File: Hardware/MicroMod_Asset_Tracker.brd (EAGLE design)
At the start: 76.2 x 76.2 mm, 338 parts, among them IC1 SN74AVC4T774PW, IC2 SN74AVC4T774PW, IC3 SN74AVC4T774PW, J11 microSD, J13 TP, J17 NANO_SIM, J18 SARA_USB, J19 NI, J2 JTAG, J4 MICROMOD-2222-C, J5 SPI, J6 DIAG, J7 QWIIC_RIGHT_ANGLE, J9 !RST!, Q1 310mA/60V/1.6Ω, Q10 20V/0.2A/8MHz/1.2Ω/1Vth, Q2 310mA/60V/1.6Ω, Q3 310mA/60V/1.6Ω, Q4 310mA/60V/1.6Ω, Q5 20V/0.2A/8MHz/1.2Ω/1Vth, Q6 20V/4.2A/52mΩ/1.4W, Q7 310mA/60V/1.6Ω, Q8 310mA/60V/1.6Ω, Q9 310mA/60V/1.6Ω, U1 SARA-R5, U13 9DoF IMU, U14 1.8V/100mA, U2 MCP73831, U3 3.3V, U5 AP7361C-33FGE, U7 PCA9306, U8 74HC1G04

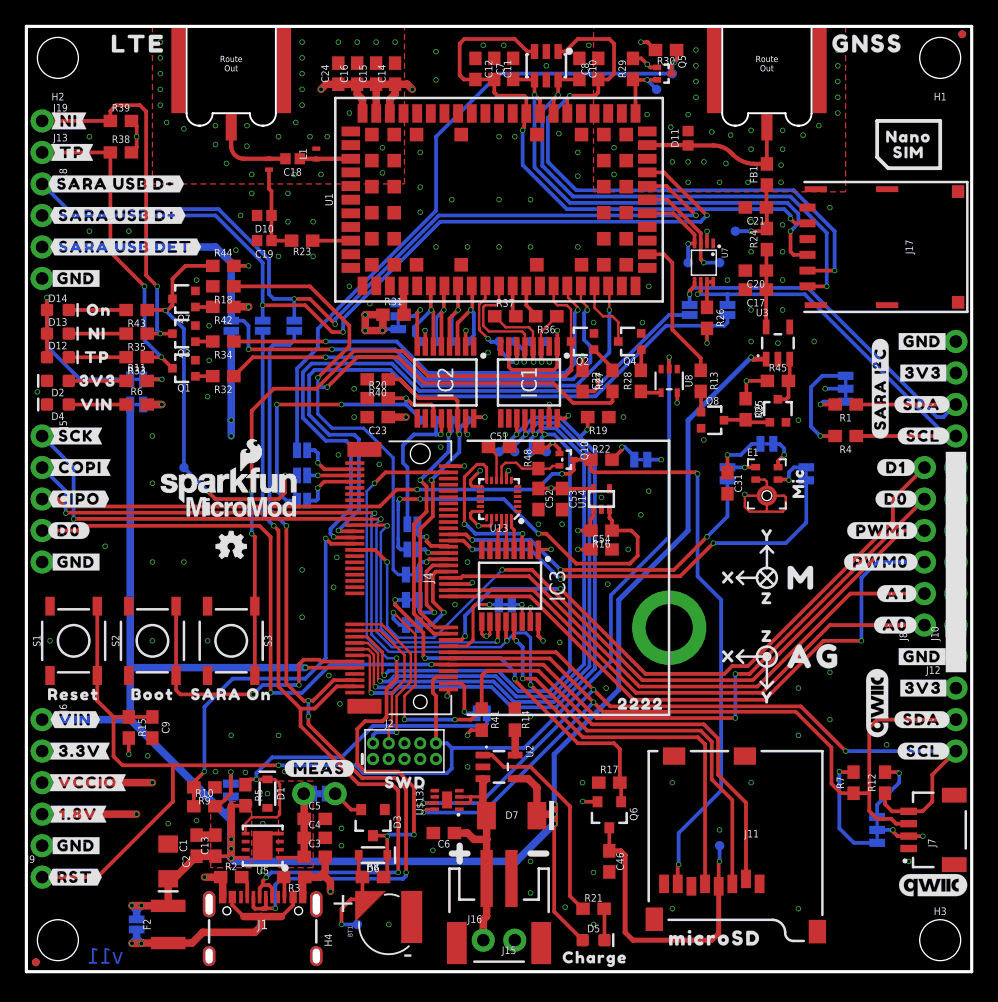
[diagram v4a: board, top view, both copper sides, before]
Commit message: Updated files for v11 after production review
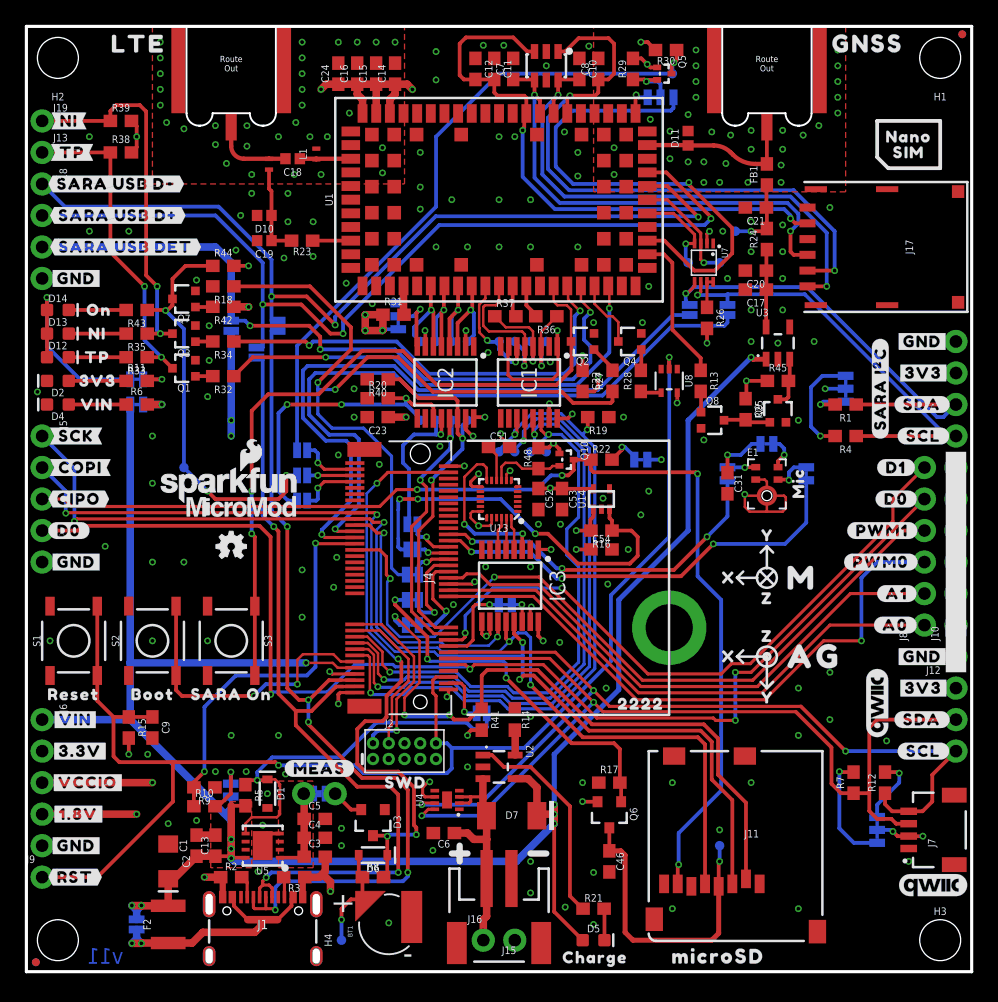
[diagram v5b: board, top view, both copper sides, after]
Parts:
- removed TP11: TEST-POINT3, SparkFun-Connectors:PAD.03X.03
- added JP19: JUMPER-SMT_3_1-NC_TRACE_SILK, SparkFun-Jumpers:SMT-JUMPER_3_1-NC_TRACE_SILK
- added U$118: (no value), output:#EXT_INT#0
- added U$119: (no value), output:#GPIO3#0
- moved U$93 2.22 mm to (18.5, 46.0)
- moved JP4 2.22 mm to (18.5, 49.9)
- moved TP24 1.80 mm to (25.4, 2.54)
- moved U$28 1.48 mm to (51.1, 1.24)
- moved JP3 1.33 mm to (20.3, 52.1)
- moved U$92 1.14 mm to (20.4, 48.1)
- moved U$103 0.14 mm to (17.2, 41.9)
- moved U$129 0.14 mm to (24.6, 41.9)
- renumbered U$132 to U4
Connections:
- removed net SARA_INT_1.8V: Q5.2, R29.1, TP11.P$1, U1.33
- new net N$43: JP19.2, Q5.2, R29.1
- new net SARA_EXT_INT: JP19.3, U1.33
- new net SARA_GPIO3: JP19.1, U1.24
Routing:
- net SARA_GPIO3: track 0.00 -> 41.1 mm, vias 0 -> 1
- net GND: track 33.4 -> 41.7 mm, vias 195 -> 198
- net SARA_INT_1.8V: track 5.91 -> 0.00 mm, vias 1 -> 0
- net N$43: track 0.00 -> 4.37 mm, vias 0 -> 1
- net SARA_USB_D+: track 71.5 -> 75.0 mm
- net D0: track 96.3 -> 99.1 mm
- net VCCIO: track 161.3 -> 163.8 mm
- net SARA_EXT_INT: track 0.00 -> 2.52 mm, vias 0 -> 1
- net SARA_USB_D-: track 69.6 -> 71.0 mm
- net CTS1: track 50.4 -> 51.7 mm
- net RX1: track 44.6 -> 45.8 mm
- net USB_D+: track 69.1 -> 67.9 mm
- net N$17: track 53.3 -> 54.2 mm
- net USB_D-: track 72.8 -> 72.0 mm
- net ICM_!CS!: track 22.6 -> 21.8 mm
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
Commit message: Adding production files for v11
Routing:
- net VCCIO: track 163.8 -> 163.0 mm

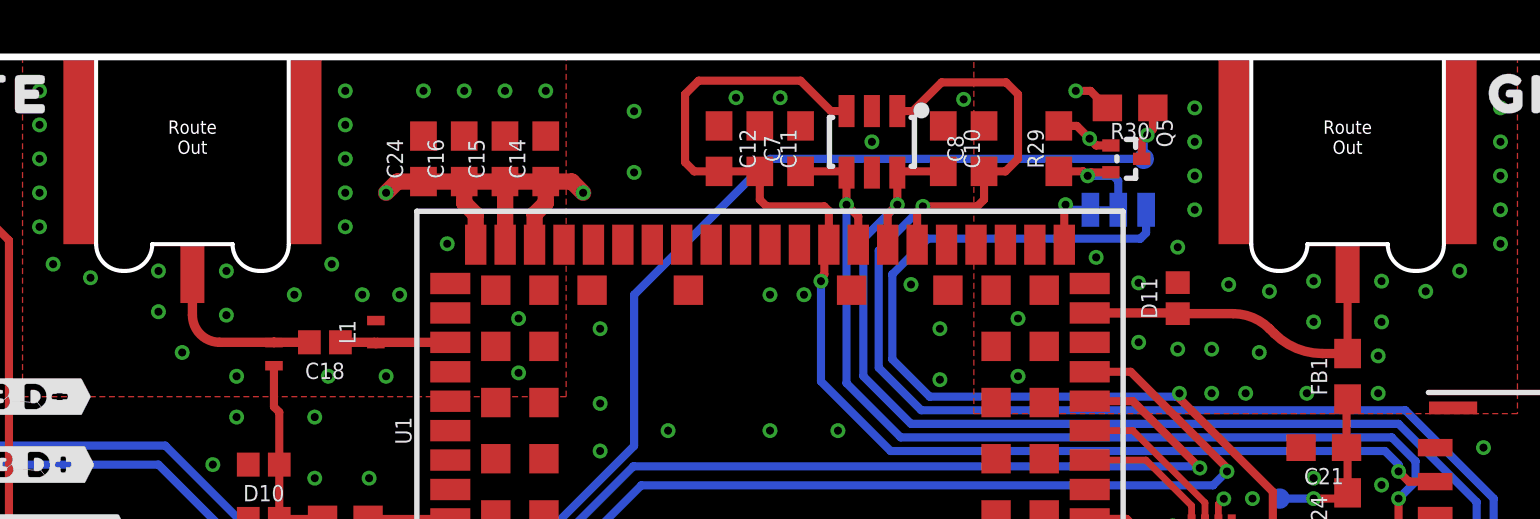
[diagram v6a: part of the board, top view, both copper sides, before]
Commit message: Adding the PROD_ID for the SARA-R510M8S
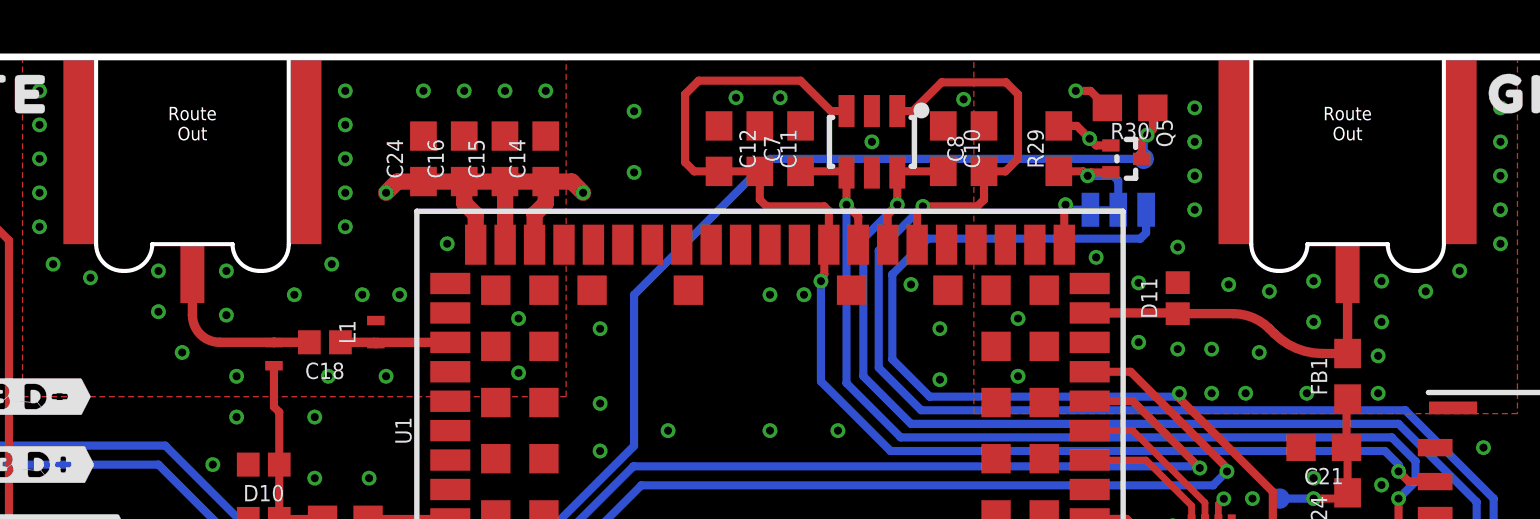
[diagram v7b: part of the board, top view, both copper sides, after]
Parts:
- E3: value LTE -> ANTENNA-SMA-GROUNDEDEDGE_SMA_SMD
- E4: value GNSS -> ANTENNA-SMA-GROUNDEDEDGE_SMA_SMD
- U1: value SARA-R5 -> SARA-R510M8S
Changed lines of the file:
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@@
 <attribute name="VALUE" x="9.398" y="19.685" size="0.6096" layer="27" font="vector" ratio="20" rot="R270" align="top-center"/>
 </element>
-<element name="U1" library="SARA_R5" package="SARA-LGA" value="SARA-R5" x="38.1" y="62.23" smashed="yes">
+<element name="U1" library="SARA_R5" package="SARA-LGA" value="SARA-R510M8S" x="38.1" y="62.23" smashed="yes">
 <attribute name="NAME" x="24.7" y="62.23" size="0.6096" layer="25" font="vector" ratio="20" rot="R90" align="bottom-center"/>
-<attribute name="PROD_ID" value="" x="38.1" y="62.23" size="1.778" layer="27" ratio="15" display="off"/>
-<attribute name="VALUE" x="51.5" y="63.23" size="0.6096" layer="27" font="vector" ratio="20" rot="R270" align="bottom-center"/>
+<attribute name="PROD_ID" value="IC-15573" x="38.1" y="62.23" size="1.778" layer="27" ratio="15" display="off"/>
+<attribute name="VALUE" value="SARA-R510M8S" x="51.5" y="63.23" size="0.6096" layer="27" font="vector" ratio="20" rot="R270" align="bottom-center"/>
 </element>
 <element name="U13" library="SparkFun-Sensors" package="QFN24-3X3-ICM-20948" value="9DoF IMU" x="38.1" y="38.1" smashed="yes" rot="R180">
@@
 <attribute name="PROD_ID" value="RES-08272" x="59.055" y="-0.508" size="1.778" layer="27" ratio="15" rot="R90" display="off"/>
 <attribute name="VALUE" x="41.837" y="41.402" size="0.6096" layer="27" font="vector" ratio="20" rot="R90" align="top-center"/>
-</element>
-<element name="E3" library="SparkFun-RF" package="SMA-EDGE-SMD" value="LTE" x="16.51" y="76.2" smashed="yes">
-<attribute name="PROD_ID" value="CONN-15100" x="5.08" y="92.71" size="1.778" layer="27" ratio="15" display="off"/>
-</element>
-<element name="E4" library="SparkFun-RF" package="SMA-EDGE-SMD" value="GNSS" x="59.69" y="76.2" smashed="yes">
-<attribute name="PROD_ID" value="CONN-15100" x="59.69" y="76.2" size="1.778" layer="27" ratio="15" display="off"/>
 </element>
 <element name="U2" library="SparkFun-IC-Power" package="SOT23-5" value="MCP73831" x="38.1" y="16.51" smashed="yes" rot="R270">
@@
 <element name="U$118" library="output" package="#EXT_INT#0" value="" x="50.2285" y="66.1035" smashed="yes" rot="MR270"/>
 <element name="U$119" library="output" package="#GPIO3#0" value="" x="52.07" y="66.929" smashed="yes" rot="MR270"/>
+<element name="E3" library="SparkFun-RF" package="SMA-EDGE-SMD" value="ANTENNA-SMA-GROUNDEDEDGE_SMA_SMD" x="16.51" y="76.2" smashed="yes">
+<attribute name="PROD_ID" value="CONN-15100" x="16.51" y="76.2" size="1.778" layer="27" ratio="15" display="off"/>
+</element>
+<element name="E4" library="SparkFun-RF" package="SMA-EDGE-SMD" value="ANTENNA-SMA-GROUNDEDEDGE_SMA_SMD" x="59.69" y="76.2" smashed="yes">
+<attribute name="PROD_ID" value="CONN-15100" x="59.69" y="76.2" size="1.778" layer="27" ratio="15" display="off"/>
+</element>
 </elements>
 <signals>
@@
 <contactref element="U14" pad="2"/>
 <contactref element="C54" pad="2"/>
-<contactref element="E4" pad="GND@1"/>
-<contactref element="E4" pad="GND@0"/>
-<contactref element="E3" pad="GND@1"/>
-<contactref element="E3" pad="GND@0"/>
 <contactref element="U1" pad="81" route="any" routetag="G$2.GND"/>
 <contactref element="U1" pad="43" route="any" routetag="G$2.GND"/>
@@
 <via x="40.64" y="32.639" extent="1-16" drill="0.3"/>
 <via x="56.134" y="59.69" extent="1-16" drill="0.3"/>
+<contactref element="E3" pad="GND@0"/>
+<contactref element="E3" pad="GND@1"/>
+<contactref element="E4" pad="GND@0"/>
+<contactref element="E4" pad="GND@1"/>
 </signal>
 <signal name="3.3V">
@@
 <polygon width="0.1778" layer="15" pour="cutout" isolate="0.2032">
 <vertex x="11.43" y="76.2"/>
-<vertex x="11.43" y="67.945"/>
-<vertex x="21.59" y="67.945"/>
+<vertex x="11.43" y="67.31"/>
+<vertex x="21.59" y="67.31"/>
 <vertex x="21.59" y="76.2"/>
 </polygon>
 <polygon width="0.1778" layer="15" pour="cutout" isolate="0.2032">
 <vertex x="54.61" y="76.2"/>
-<vertex x="54.61" y="67.945"/>
-<vertex x="64.77" y="67.945"/>
+<vertex x="54.61" y="67.31"/>
+<vertex x="64.77" y="67.31"/>
 <vertex x="64.77" y="76.2"/>
 </polygon>
@@
 <signal name="SARA_ANT_GNSS">
 <contactref element="U1" pad="31"/>
-<contactref element="E4" pad="SIG"/>
 <contactref element="FB1" pad="2"/>
 <contactref element="D11" pad="1"/>
 <wire x1="50.05" y1="66.63" x2="53.313" y2="66.63" width="0.35051875" layer="1"/>
 <wire x1="53.313" y1="66.63" x2="53.34" y2="66.603" width="0.35051875" layer="1"/>
-<wire x1="59.69" y1="65.112" x2="59.69" y2="68.1" width="0.3048" layer="1"/>
 <wire x1="53.34" y1="66.603" x2="55.409796875" y2="66.603" width="0.35051875" layer="1"/>
 <wire x1="55.409796875" y1="66.603" x2="56.769" y2="66.04" width="0.35051875" layer="1" curve="-45"/>
@@
 <wire x1="56.95305" y1="65.85595" x2="58.749103125" y2="65.112" width="0.35051875" layer="1" curve="45"/>
 <wire x1="58.749103125" y1="65.112" x2="59.69" y2="65.112" width="0.35051875" layer="1"/>
+<contactref element="E4" pad="SIG"/>
+<wire x1="59.69" y1="65.112" x2="59.69" y2="68.1" width="0.35051875" layer="1"/>
 </signal>
 <signal name="N$15">
 <contactref element="C18" pad="2"/>
-<contactref element="E3" pad="SIG"/>
 <contactref element="L2" pad="P$2"/>
-<wire x1="16.51" y1="66.548" x2="17.526" y2="65.532" width="0.35051875" layer="1" curve="90"/>
-<wire x1="16.51" y1="66.548" x2="16.51" y2="68.1" width="0.35051875" layer="1"/>
+<wire x1="17.526" y1="65.532" x2="16.51" y2="66.548" width="0.35051875" layer="1" curve="-90"/>
 <wire x1="17.526" y1="65.532" x2="19.5453" y2="65.532" width="0.35051875" layer="1"/>
 <wire x1="19.5453" y1="65.532" x2="19.558" y2="65.5193" width="0.35051875" layer="1"/>
 <wire x1="19.558" y1="65.5193" x2="19.5707" y2="65.532" width="0.35051875" layer="1"/>
 <wire x1="19.5707" y1="65.532" x2="20.883" y2="65.532" width="0.35051875" layer="1"/>
+<contactref element="E3" pad="SIG"/>
+<wire x1="16.51" y1="66.548" x2="16.51" y2="68.1" width="0.35051875" layer="1"/>
 </signal>
 <signal name="N$16">
